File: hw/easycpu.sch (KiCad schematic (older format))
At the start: 0 parts

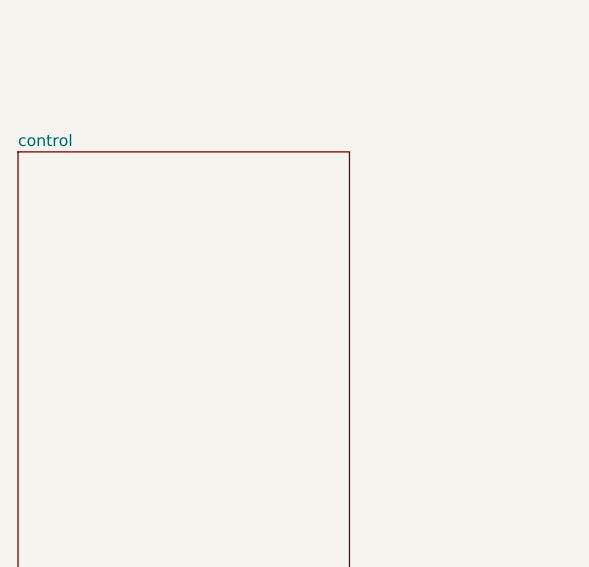
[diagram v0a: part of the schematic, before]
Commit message: annotate control schematic, add other 74HC74 units
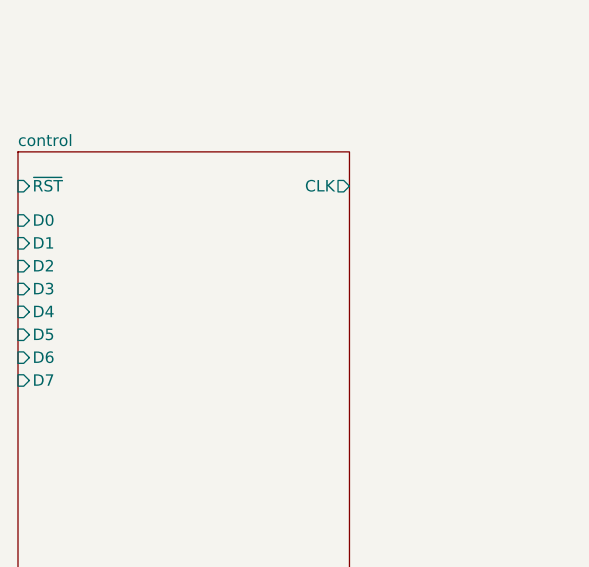
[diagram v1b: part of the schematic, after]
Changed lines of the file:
@@
 F0 "control" 50
 F1 "control.sch" 50
+F2 "~RST" I L 3600 6350 50
+F3 "CLK" O R 5050 6350 50
+F4 "D0" I L 3600 6500 50
+F5 "D1" I L 3600 6600 50
+F6 "D2" I L 3600 6700 50
+F7 "D3" I L 3600 6800 50
+F8 "D4" I L 3600 6900 50
+F9 "D5" I L 3600 7000 50
+F10 "D6" I L 3600 7100 50
+F11 "D7" I L 3600 7200 50
 $EndSheet
 $EndSCHEMATC

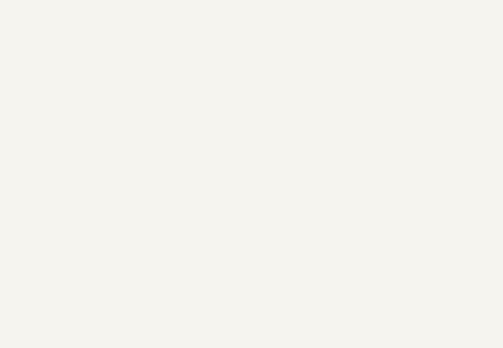
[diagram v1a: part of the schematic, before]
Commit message: added reset unit, some cleanups of control unit
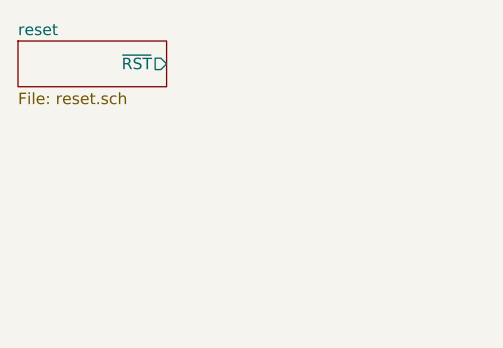
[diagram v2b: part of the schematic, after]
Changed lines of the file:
@@
 $Descr User 13750 10625
 encoding utf-8
-Sheet 1 3
+Sheet 1 4
 Title ""
 Date ""
@@
 F11 "D7" I L 3600 7200 50
 $EndSheet
+$Sheet
+S 1800 1400 650  200
+U 5DACE71F
+F0 "reset" 50
+F1 "reset.sch" 50
+F2 "~RST" O R 2450 1500 50
+$EndSheet
 $EndSCHEMATC
